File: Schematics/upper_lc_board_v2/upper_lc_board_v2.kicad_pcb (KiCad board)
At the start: 4 copper layers, 69.5 x 60 mm, 115 parts, among them J1 USB_C_Female_USB2_Small, J2 Stack Male Edge Connector, J3 PT1, J4 PT1, J5 HALL-1, J6 SOL_CONN, J7 SOL_CONN, Q1 AO3400A, Q2 AO3400A, Q4 2N7002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

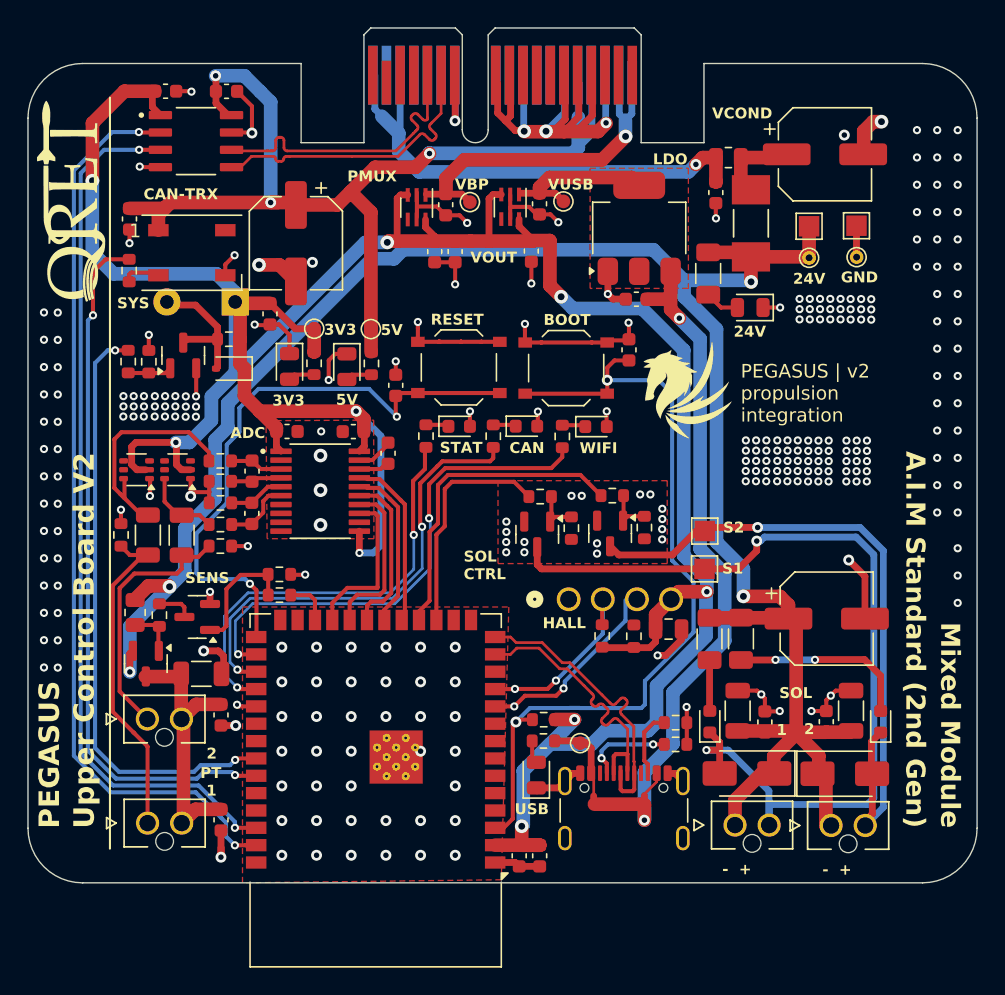
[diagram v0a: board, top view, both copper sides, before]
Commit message: layout updates after review, cleaned up schematic organization
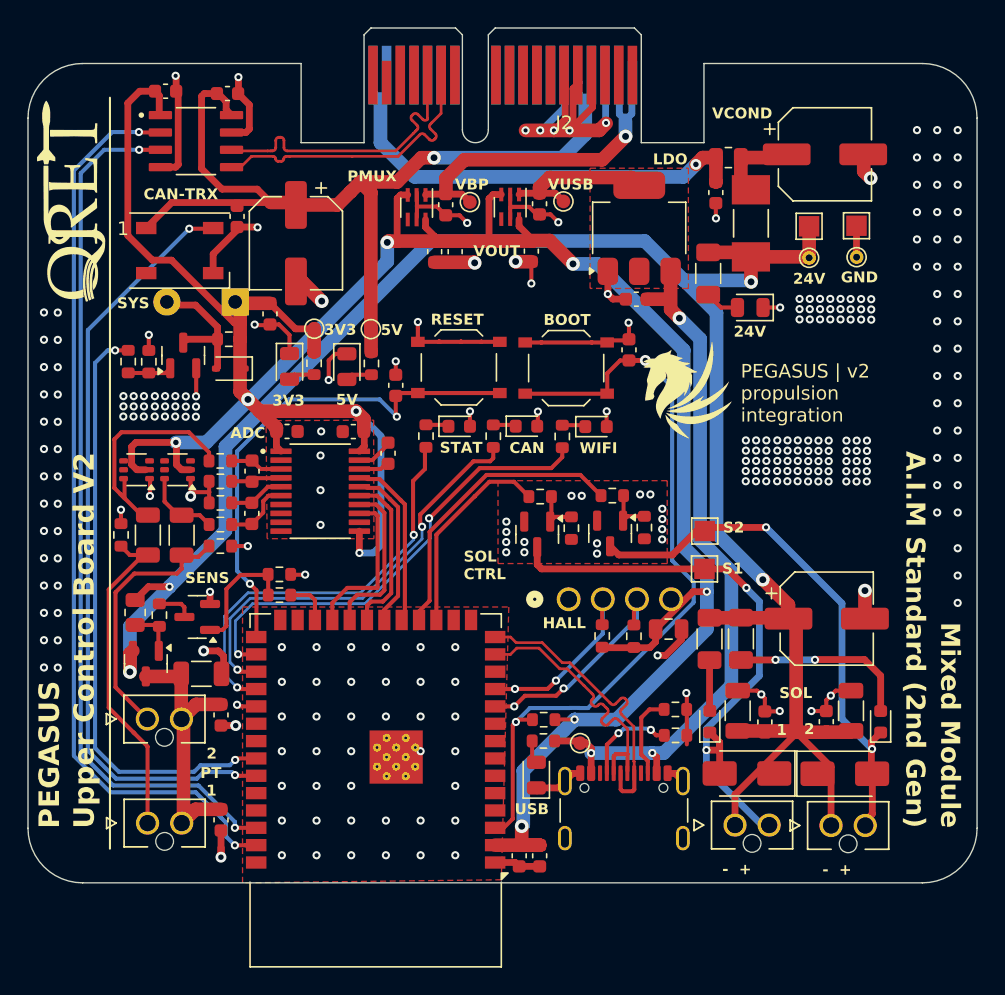
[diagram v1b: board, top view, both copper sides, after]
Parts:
- removed R30: 470, Resistor_SMD:R_0603_1608Metric
- moved C27 7.88 mm to (123.3, 71.2)
- moved R6 0.97 mm to (155.4, 107.3)
- moved D4 0.90 mm to (119.1, 73.7)
- moved R5 0.66 mm to (155.4, 109.2)
- moved C7 0.17 mm to (122.6, 62.2)
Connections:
- D4 pad 2: Net-(D4-DOUT) -> unconnected-(D4-DOUT-Pad2)
- J2 pad A12: GND -> unconnected-(J2-GND_B-PadA12)_3
- J2 pad A16: +24V_BP -> unconnected-(J2-Reserved-PadA16)
- J2 pad A17: unconnected-(J2-Reserved-PadA17) -> +24V_BP
- J2 pad A9: GND -> unconnected-(J2-GND_B-PadA12)_2
- J2 pad B10: GND -> unconnected-(J2-GND_B-PadA12)_4
- J2 pad B11: GND -> unconnected-(J2-GND_B-PadA12)_1
- J2 pad B12: GND -> unconnected-(J2-GND_B-PadA12)
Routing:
- net SOL1_RET: track 68.4 -> 43.7 mm
- net GND: track 167.6 -> 152.0 mm, vias 280 -> 277
- net +3V3: track 215.9 -> 201.6 mm
- net SOL2_RET: track 49.5 -> 39.0 mm, vias 1 -> 2
- net 5V_USB: track 60.2 -> 52.3 mm, vias 2 -> 3
- net +5V: track 77.0 -> 69.3 mm, vias 3 -> 1
- net /ESP32-S3 Breakout Circuitry/ESP32_IO0: track 44.0 -> 37.3 mm
- net /ESP32-S3 Breakout Circuitry/GPIO_42: track 52.0 -> 56.8 mm
- net Net-(D4-DOUT): track 2.81 -> 0.00 mm
- net /ESP32-S3 Breakout Circuitry/GPIO_35: track 37.0 -> 34.2 mm
- net /ESP32-S3 Breakout Circuitry/GPIO_36: track 34.2 -> 31.6 mm
- net HALL_SDA: track 13.9 -> 16.4 mm
- net +24V: track 152.0 -> 149.6 mm
- net /ESP32-S3 Breakout Circuitry/ESP32_EN: track 59.7 -> 57.7 mm
- net VALVE2_CTRL: track 23.3 -> 21.7 mm
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
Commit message: swap I2C lines, add digi numbers to conns, fix diode issue
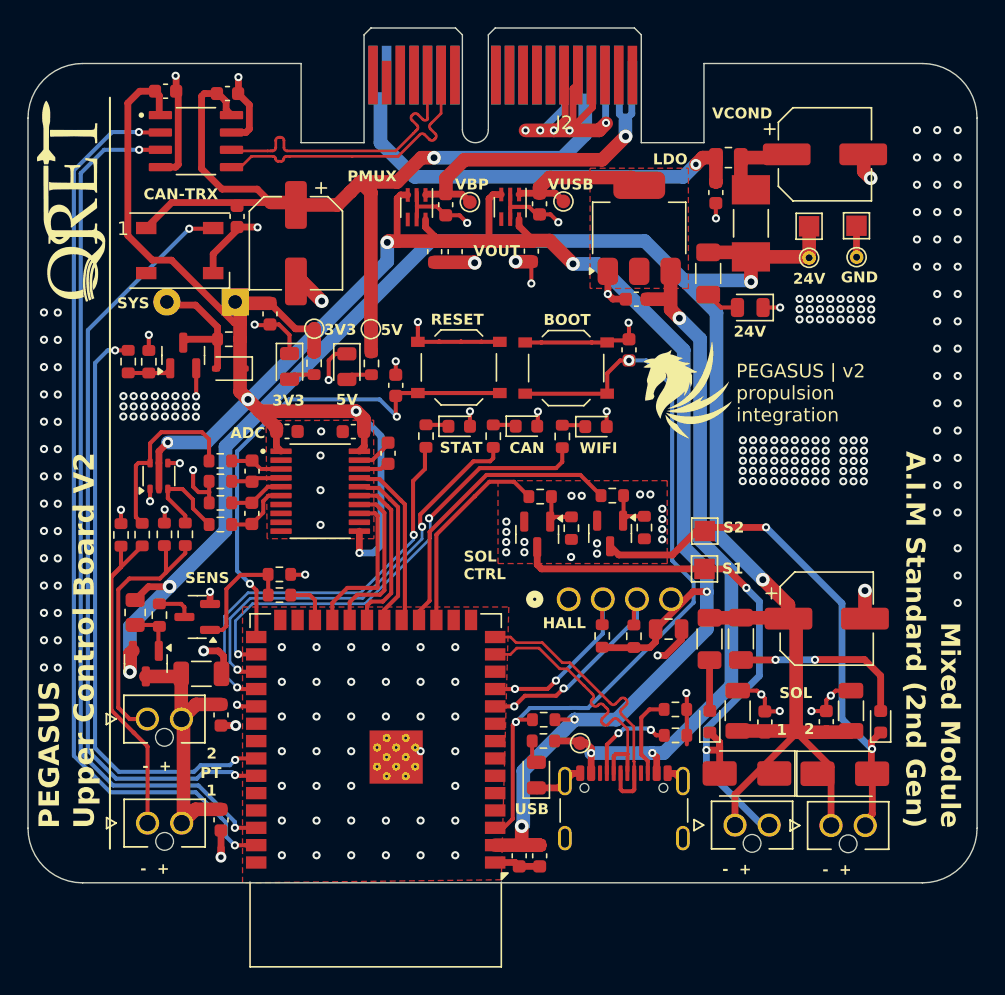
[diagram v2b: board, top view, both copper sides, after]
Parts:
- removed D12: BAV199DW, Package_TO_SOT_SMD:SOT-363_SC-70-6
- R12, R17: footprint Resistor_SMD:R_1206_3216Metric -> Resistor_SMD:R_0603_1608Metric
- moved R14 4.18 mm to (118.0, 94.5), turned to -90 degrees
- moved R21 2.32 mm to (150.0, 101.9)
- moved R22 2.32 mm to (152.4, 101.9)
- moved D11 1.70 mm to (117.6, 90.2), turned to 90 degrees
- moved R12 0.42 mm to (116.3, 94.5)
- moved R17 0.28 mm to (119.5, 94.5)
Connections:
- D11 pad 3: (no net) -> Net-(D11B-K1A2)
- D11 pad 4: (no net) -> GND
- D11 pad 5: (no net) -> +3V3
- J5 pad 2: HALL_SCL -> HALL_SDA
- J5 pad 3: HALL_SDA -> HALL_SCL
- R17 pad 2: Net-(D12A-K3A4) -> Net-(D11B-K1A2)
- R18 pad 2: Net-(D12A-K3A4) -> Net-(D11B-K1A2)
- U1 pad 10: HALL_SDA -> HALL_SCL
- U1 pad 11: HALL_SCL -> HALL_SDA
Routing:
- net Net-(D11B-K1A2): track 0.00 -> 7.50 mm
- net Net-(D12A-K3A4): track 5.64 -> 0.00 mm
- net +3V3: track 201.6 -> 197.3 mm
- net Net-(D11A-K3A4): track 17.1 -> 13.5 mm
- net HALL_SDA: track 16.4 -> 13.9 mm
- net HALL_SCL: track 13.9 -> 16.4 mm
- net /ESP32-S3 Breakout Circuitry/ESP32_EN: track 57.7 -> 56.6 mm
- net /Sensing Circuitry/PT2: track 19.2 -> 19.7 mm
- net GND: track 152.0 -> 152.1 mm, vias 277 -> 279

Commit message: resolve DRC & tweak
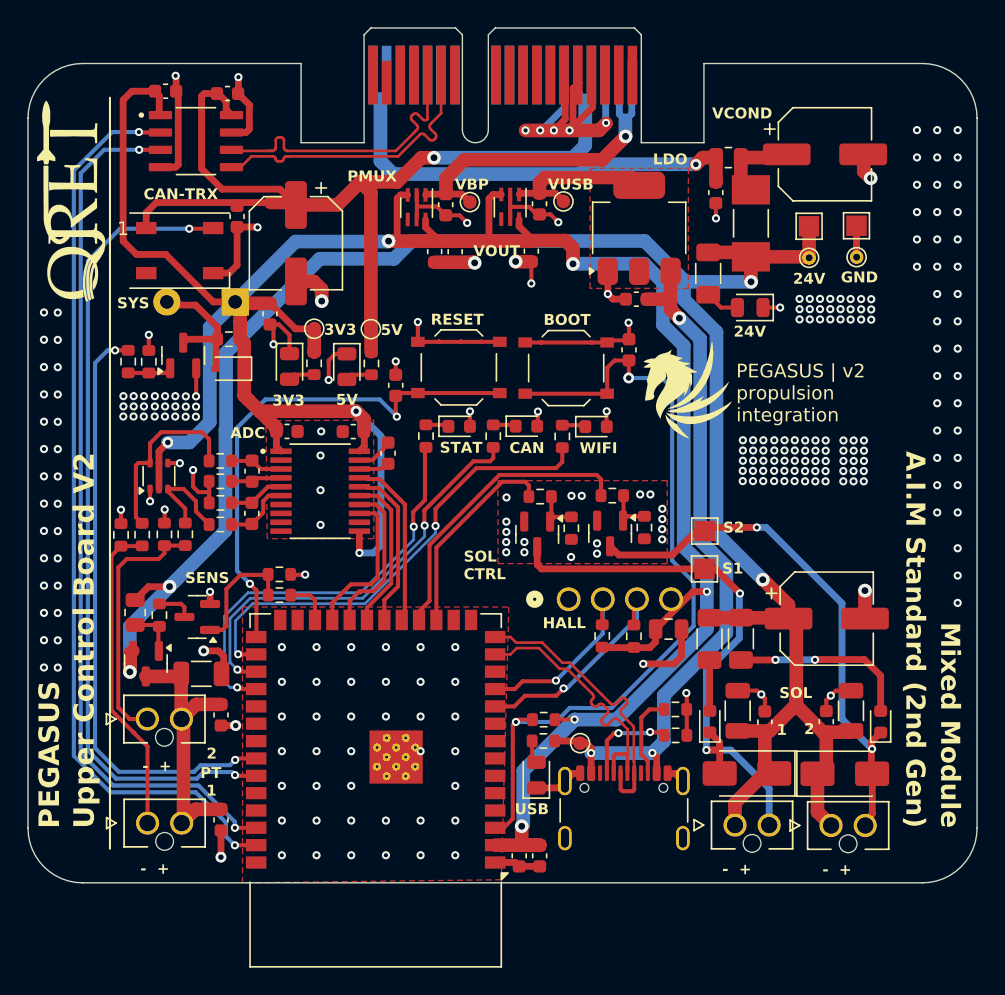
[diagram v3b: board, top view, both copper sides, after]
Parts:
- R11, R14: value 60 -> 62
- moved D15 0.06 mm to (122.8, 82.3)
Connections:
- D4 pad 4: unconnected-(D4-DIN-Pad4) -> /ESP32-S3 Breakout Circuitry/GPIO_42
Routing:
- net +3V3: track 197.3 -> 205.0 mm, vias 9 -> 8
- net +5V: track 69.3 -> 74.3 mm
- net +24V: track 149.6 -> 152.7 mm
- net /ESP32-S3 Breakout Circuitry/GPIO_42: track 56.8 -> 59.8 mm
- net /ESP32-S3 Breakout Circuitry/ESP32_EN: track 56.6 -> 58.5 mm
- net /Sensing Circuitry/PT1: track 25.0 -> 23.4 mm
- net /ESP32-S3 Breakout Circuitry/GPIO_38: track 1.45 -> 0.00 mm, vias 1 -> 0
- net /ESP32-S3 Breakout Circuitry/ESP32_IO0: track 37.3 -> 38.3 mm
- net SOL1_RET: track 43.7 -> 42.8 mm
- net /Sensing Circuitry/PT2: track 19.7 -> 18.8 mm
- net 5V_USB: track 52.3 -> 51.5 mm
- net +24V_BP: track 35.0 -> 35.7 mm
- net GND: track 152.1 -> 152.2 mm, vias 279 -> 278
- net HALL_SDA: vias 2 -> 1
- net HALL_SCL: vias 2 -> 1

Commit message: updated pcb after part number and schematic fixes
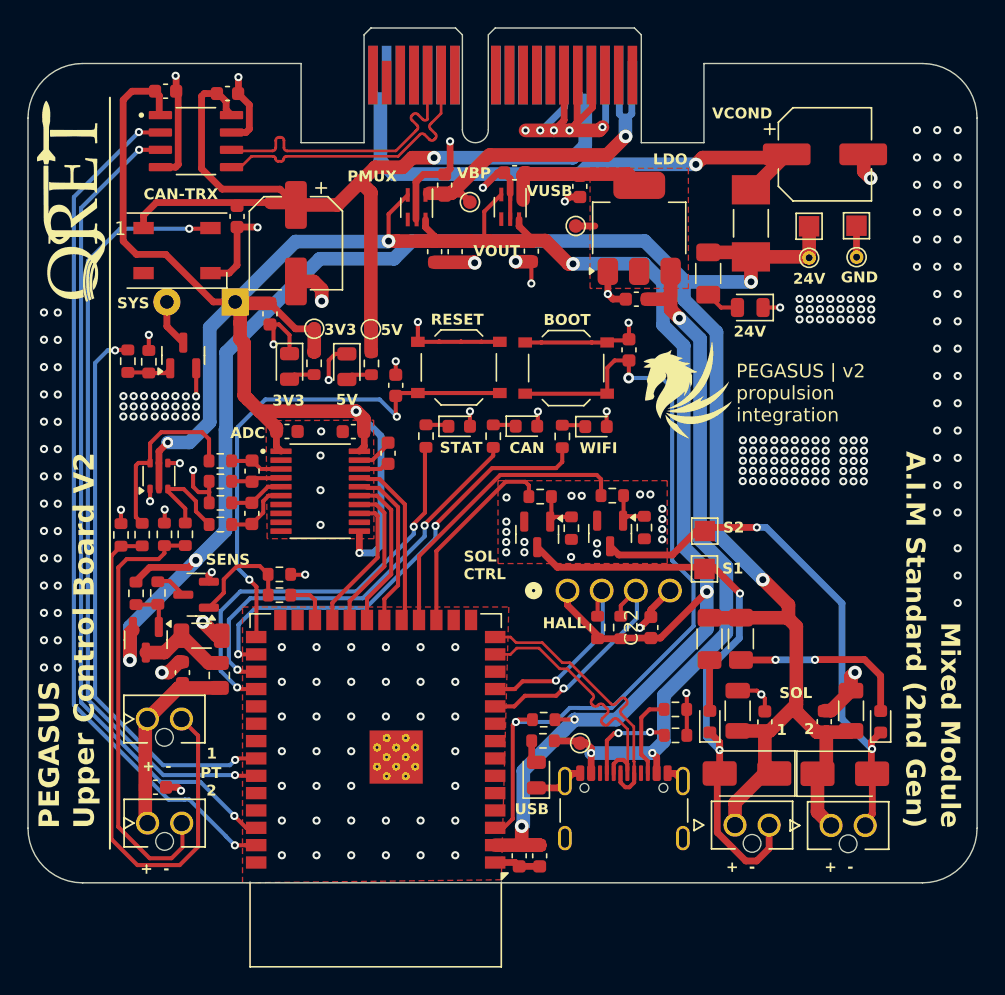
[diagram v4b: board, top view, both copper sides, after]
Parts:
- removed C28: 0.1uF, Capacitor_SMD:C_0603_1608Metric
- removed D15: 1N4148WS-7-F, Diode_SMD:D_SOD-323
- removed R27: 220, Resistor_SMD:R_0603_1608Metric
- C10: value 100uF -> 100uF 16V
- C13: value 100uF -> 0.1uF; footprint Capacitor_SMD:CP_Elec_6.3x5.9 -> Capacitor_SMD:C_0603_1608Metric
- C22: footprint Capacitor_SMD:C_0805_2012Metric -> Capacitor_SMD:C_0603_1608Metric
- C5: value 0.1uF -> 10uF
- C9: value 100uF -> 100uF 35V
- D1: value FAULT_LED -> FAULT_LED (RED)
- D10: value SOL1_LED (YELW) -> SOL1_LED (WHT)
- D2: value CAN_LED -> CAN_LED (WHT)
- D3: value WIFI_LED -> WIFI_LED (WHT)
- D9: value SOL2_LED (YELW) -> SOL2_LED (WHT)
- FB1: value FerriteBead -> 100R
- R10: value 330 -> 200
- R15, R16, R8: value 4.7k -> 12k
- R2: value 150 -> 680
- R28: value 10K -> 10k
- R29: value 1k -> 6.2k
- R3, R4: value 150 -> 270
- R37: value 4.7K -> 6.2k; footprint Resistor_SMD:R_0805_2012Metric -> Resistor_SMD:R_0603_1608Metric
- R7: value 220 -> 3.3k
- R9: value 510 -> 6.2k
- U3: value AMS1117 -> AMS1117-3.3
- moved FB1 53.2 mm to (122.0, 104.8), turned to -90 degrees
- moved C8 52.5 mm to (119.3, 104.6), turned to 90 degrees
- moved C13 50.7 mm to (117.3, 113.0)
- moved C5 46.8 mm to (148.4, 69.0)
- moved R10 41.2 mm to (115.3, 81.8), turned to 90 degrees
- moved R29 37.3 mm to (145.7, 109.6), turned to 180 degrees
- moved C12 2.92 mm to (143.6, 68.0), turned to 180 degrees
- moved C24 2.80 mm to (120.7, 101.9)
- moved TP9 2.01 mm to (148.1, 71.9)
- moved U9 1.75 mm to (116.6, 102.2)
- moved Q5 1.63 mm to (120.3, 98.9)
- moved R23 1.62 mm to (117.5, 98.8)
- moved C11 1.44 mm to (138.5, 68.9), turned to -90 degrees
- moved R37 1.40 mm to (115.9, 98.8)
- moved C22 1.31 mm to (153.6, 101.3), turned to 90 degrees
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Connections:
- C13 pad 1: +24V -> VPT
- C24 pad 1: VPT -> Net-(U9-D)
- C27 pad 1: +5V -> GND
- C27 pad 2: GND -> +5V
- C5 pad 1: VPT -> /Power Circuitry/3V3_USB
- C8 pad 1: +24V_BP -> VPT
- C9 pad 1: Net-(C9-Pad1) -> +24V_BP
- F1 pad 2: Net-(C9-Pad1) -> +24V_BP
- FB1 pad 1: +24V_BP -> Net-(U9-D)
- FB1 pad 2: Net-(C9-Pad1) -> VPT
- J3 pad 1: /Sensing Circuitry/PT1 -> VPT
- J3 pad 2: VPT -> Net-(J3-Pin_2)
- J4 pad 1: /Sensing Circuitry/PT2 -> VPT
- J4 pad 2: VPT -> Net-(J4-Pin_2)
- J5 pad 1: GND -> +3V3
- J5 pad 4: +3V3 -> GND
- R10 pad 1: 5V_USB -> Net-(Q4-G)
- R10 pad 2: Net-(D8-A) -> BUZZ_IN
- R11 pad 2: /Sensing Circuitry/PT1 -> Net-(J4-Pin_2)
- R12 pad 1: /Sensing Circuitry/PT1 -> Net-(J4-Pin_2)
- R14 pad 2: /Sensing Circuitry/PT2 -> Net-(J3-Pin_2)
- R17 pad 1: /Sensing Circuitry/PT2 -> Net-(J3-Pin_2)
- R29 pad 1: Net-(BZ1--) -> 5V_USB
- R29 pad 2: +3V3 -> Net-(D8-A)
- U9 pad 3: VPT -> Net-(U9-D)
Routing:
- net Net-(J4-Pin_2): track 0.00 -> 40.8 mm
- net Net-(J3-Pin_2): track 0.00 -> 32.6 mm
- net /Sensing Circuitry/PT1: track 23.4 -> 0.00 mm
- net /Sensing Circuitry/PT2: track 18.8 -> 0.00 mm
- net Net-(U9-D): track 0.00 -> 6.69 mm
- net VPT: track 20.4 -> 13.7 mm
- net Net-(BZ1--): track 10.1 -> 3.48 mm
- net Net-(C9-Pad1): track 6.16 -> 0.00 mm
- net GND: track 152.2 -> 147.7 mm, vias 278 -> 276
- net +24V_BP: track 35.7 -> 39.8 mm
- net /ESP32-S3 Breakout Circuitry/GPIO_01: track 67.1 -> 63.1 mm
- net /ESP32-S3 Breakout Circuitry/GPIO_02: track 64.4 -> 60.4 mm
- net /ESP32-S3 Breakout Circuitry/GPIO_42: track 59.8 -> 56.7 mm
- net +5V: track 74.3 -> 71.4 mm
- net BUZZ_IN: track 43.9 -> 41.3 mm
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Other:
- board text added: "+ -"
- board text removed: "- +"

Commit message: updated silkscree and changed PI caps
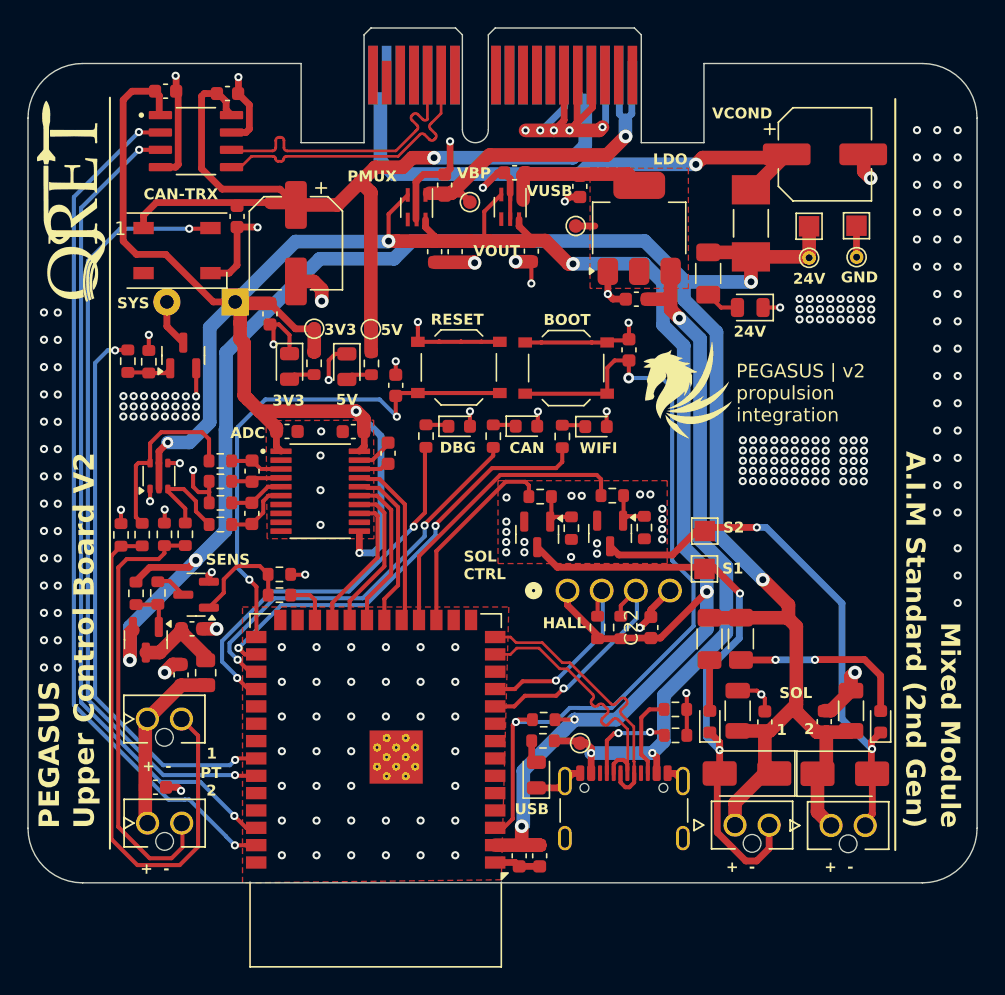
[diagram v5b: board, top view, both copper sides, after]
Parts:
- C24: value 10uF -> 0.1uF; footprint Capacitor_SMD:C_1206_3216Metric -> Capacitor_SMD:C_0603_1608Metric
- C8: value 0.1uF -> 10uF
- moved C8 3.28 mm to (120.0, 101.4), turned to 0 degrees
- moved C24 3.24 mm to (119.2, 104.8), turned to 90 degrees
- moved FB1 1.02 mm to (121.0, 104.6)
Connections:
- C24 pad 1: Net-(U9-D) -> VPT
- C8 pad 1: VPT -> Net-(U9-D)
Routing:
- net /ESP32-S3 Breakout Circuitry/GPIO_37: track 30.6 -> 28.5 mm
- net /ESP32-S3 Breakout Circuitry/GPIO_36: track 30.8 -> 29.3 mm
- net /ESP32-S3 Breakout Circuitry/GPIO_35: track 33.6 -> 32.3 mm
- net GND: track 147.7 -> 146.5 mm
- net VPT: track 13.7 -> 12.9 mm
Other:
- board text added: "+ SC SD -"
- board text added: "DBG"
- board text removed: "+ SD SC -"
- board text removed: "STAT"

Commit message: final silkscreen
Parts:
- added G***: LOGO, LOGO, B.Cu at (120.3, 65.7)
- moved G*** 1.26 mm to (156.2, 85.6)
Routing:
- net SOL1_RET: track 43.7 -> 44.9 mm
- net +24V: track 153.3 -> 154.2 mm
- net +3V3: track 206.7 -> 206.1 mm
- net GND: track 146.5 -> 146.4 mm, vias 276 -> 275
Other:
- board text added: "- SC SD +"
- board text added: "BZ"
- board text added: "LPF"
- board text added: "PT-1"
- board text added: "PT-2"
- board text added: "Pegasus QRET March 2026 Jeevan Sanchez"
- board text added: "SOL-1"
- board text added: "SOL-2"
- board text added: "VPT SW"
- board text added: "←"
- board text removed: "+ SC SD -"
- board text removed: "Pegasus QRET Feb 2026 Jeevan Sanchez"
- board text removed: "SENS"

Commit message: silk
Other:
- board text added: "propulsion integration"
- board text added: "| v2"
- board text removed: "PEGASUS | v2 propulsion integration"
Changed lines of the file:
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@@
+		)
+	)
+	(gr_text "PEGASUS"
+		(at 160.08 84.35 0)
+		(layer "F.SilkS")
+		(effects
+			(font
+				(size 1 1)
+				(thickness 0.2)
+				(bold yes)
+			)
+			(justify left bottom)
 		)
 	)
@@
 		)
 	)
+	(gr_text "propulsion \nintegration"
+		(at 160 87.46 0)
+		(layer "F.SilkS")
+		(effects
+			(font
+				(size 1 1)
+				(thickness 0.125)
+			)
+			(justify left bottom)
+		)
+	)
 	(gr_text "2"
 		(at 121.04 113.71 0)
@@
 		)
 	)
-	(gr_text "PEGASUS | v2 \npropulsion \nintegration"
-		(at 159.91 87.59 0)
-		(layer "F.SilkS")
-		(effects
+	(gr_text "       | v2 \n"
+		(at 161.69 84.27 0)
+		(layer "F.SilkS")
+		(effects
